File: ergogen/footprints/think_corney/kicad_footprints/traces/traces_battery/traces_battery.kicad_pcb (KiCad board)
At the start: 2 copper layers, 4 parts

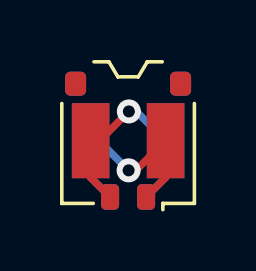
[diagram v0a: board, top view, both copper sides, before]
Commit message: Traces: Fix potential DRC clearance errors in battery footprint
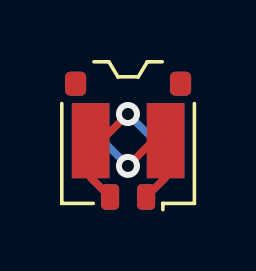
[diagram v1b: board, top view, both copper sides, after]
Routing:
- net BAT_P: track 7.61 -> 4.21 mm
- net GND: track 7.60 -> 4.36 mm
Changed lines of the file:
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@@
       (net 2 "BAT_P"))
   )
-  (segment (start -0.949808 0) (end 0.025498 -0.975306) (width 0.25) (layer "F.Cu") (net 1))
+  (segment (start -0.895498 0) (end -0.005498 -0.89) (width 0.25) (layer "F.Cu") (net 1))
   (segment (start -1.25 1.225) (end -0.6 1.875) (width 0.25) (layer "F.Cu") (net 1))
-  (segment (start -1.25 0) (end -0.949808 0) (width 0.25) (layer "F.Cu") (net 1))
-  (segment (start -1.25 0) (end -1.25 1.225) (width 0.25) (layer "F.Cu") (net 1))
-  (via (at 0.025498 -0.975306) (size 0.8) (drill 0.4) (layers "F.Cu" "B.Cu") (net 1))
+  (via (at -0.005498 -0.89) (size 0.8) (drill 0.4) (layers "F.Cu" "B.Cu") (net 1))
   (segment (start 1.25 1.225) (end 0.6 1.875) (width 0.25) (layer "B.Cu") (net 1))
-  (segment (start 1.25 0) (end 1.25 1.225) (width 0.25) (layer "B.Cu") (net 1))
-  (segment (start 0.025498 -0.975306) (end 0.274694 -0.975306) (width 0.25) (layer "B.Cu") (net 1))
-  (segment (start 0.274694 -0.975306) (end 1.25 0) (width 0.25) (layer "B.Cu") (net 1))
+  (segment (start 0.884502 0) (end -0.005498 -0.89) (width 0.25) (layer "B.Cu") (net 1))
   (segment (start 1.25 1.225) (end 0.6 1.875) (width 0.25) (layer "F.Cu") (net 2))
-  (segment (start 0.261664 0.988336) (end 1.25 0) (width 0.25) (layer "F.Cu") (net 2))
-  (segment (start 1.25 0) (end 1.25 1.225) (width 0.25) (layer "F.Cu") (net 2))
-  (segment (start 0.01685 0.988336) (end 0.261664 0.988336) (width 0.25) (layer "F.Cu") (net 2))
-  (via (at 0.01685 0.988336) (size 0.8) (drill 0.4) (layers "F.Cu" "B.Cu") (net 2))
-  (segment (start -0.971486 0) (end 0.01685 0.988336) (width 0.25) (layer "B.Cu") (net 2))
-  (segment (start -1.25 0) (end -1.25 1.225) (width 0.25) (layer "B.Cu") (net 2))
-  (segment (start -1.25 0) (end -0.971486 0) (width 0.25) (layer "B.Cu") (net 2))
+  (segment (start 0.834502 0) (end -0.005498 0.84) (width 0.25) (layer "F.Cu") (net 2))
+  (via (at -0.005498 0.84) (size 0.8) (drill 0.4) (layers "F.Cu" "B.Cu") (net 2))
+  (segment (start -0.845498 0) (end -0.005498 0.84) (width 0.25) (layer "B.Cu") (net 2))
   (segment (start -1.25 1.225) (end -0.6 1.875) (width 0.25) (layer "B.Cu") (net 2))
 )
